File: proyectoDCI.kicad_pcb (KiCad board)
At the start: 2 copper layers, 50 x 30 mm, 27 parts, among them P1 CONN_02X04, P2 CONN_01X01, P3 GSG-RF-CONN, P4 GSG-RF-CONN, U1 AD5933, U2 ADG849, U3 AD8606, U4 ASFLMB-16.000MHZ-LY-T, U5 ADP150

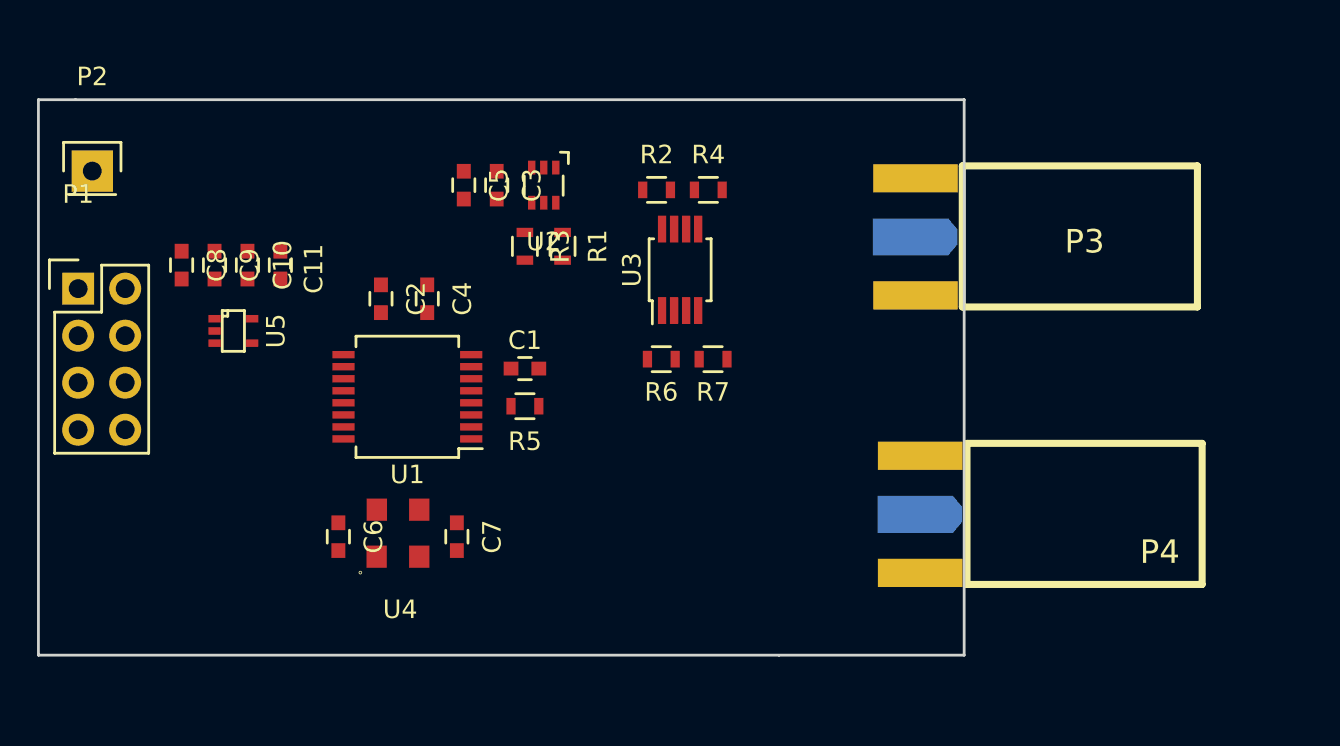
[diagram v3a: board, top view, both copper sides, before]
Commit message: Se achico el tamaño de la placa para hacerla mas compacta
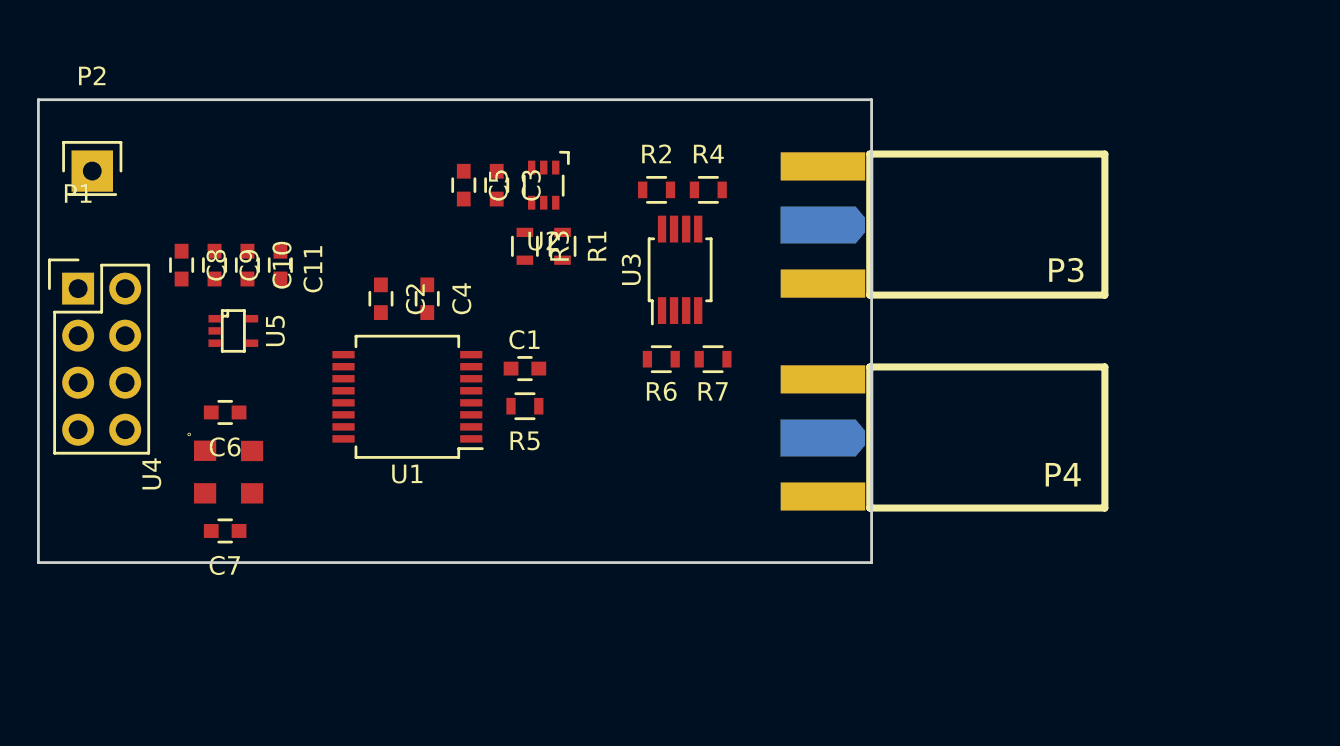
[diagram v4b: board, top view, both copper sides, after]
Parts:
- moved C7 12.5 mm to (160.1, 121.3), turned to 180 degrees
- moved U4 9.72 mm to (160.3, 118.1), turned to 270 degrees
- moved C6 9.08 mm to (160.1, 114.9), turned to 180 degrees
- moved P4 6.68 mm to (201.2, 115.0)
- moved P3 5.04 mm to (201.2, 103.5)
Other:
- board size 50 x 30 mm -> 45 x 25 mm
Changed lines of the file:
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@@
     (area 149.924999 97.924999 200.075001 128.075001)
     (thickness 1.6)
-    (drawings 36)
+    (drawings 34)
     (tracks 0)
     (zones 0)
@@
   )
   (module Capacitors_SMD:C_0603 (layer F.Cu)
-    (at 166.2 121.6 270)
+    (at 160.086 114.892 180)
     (descr "Capacitor SMD 0603, reflow soldering, AVX (see smccp.pdf)")
     (tags "capacitor 0603")
     (attr smd)
-    (fp_text reference C6 (at 0 -1.9 270) (layer F.SilkS)
-      (effects (font (size 1 1) (thickness 0.15)))
-    )
-    (fp_text value 10uF (at 0 1.9 270) (layer F.Fab)
+    (fp_text reference C6 (at 0 -1.9 180) (layer F.SilkS)
+      (effects (font (size 1 1) (thickness 0.15)))
+    )
+    (fp_text value 10uF (at 0 1.9 180) (layer F.Fab)
       (effects (font (size 1 1) (thickness 0.15)))
     )
@@
     (fp_line (start -0.35 -0.6) (end 0.35 -0.6) (layer F.SilkS) (width 0.15))
     (fp_line (start 0.35 0.6) (end -0.35 0.6) (layer F.SilkS) (width 0.15))
-    (pad 1 smd rect (at -0.75 0 270) (size 0.8 0.75) (layers F.Cu F.Paste F.Mask)
+    (pad 1 smd rect (at -0.75 0 180) (size 0.8 0.75) (layers F.Cu F.Paste F.Mask)
       (net 1 VDD))
-    (pad 2 smd rect (at 0.75 0 270) (size 0.8 0.75) (layers F.Cu F.Paste F.Mask)
+    (pad 2 smd rect (at 0.75 0 180) (size 0.8 0.75) (layers F.Cu F.Paste F.Mask)
       (net 2 GND))
     (model Capacitors_SMD.3dshapes/C_0603.wrl
@@
   )
   (module Capacitors_SMD:C_0603 (layer F.Cu)
-    (at 172.6 121.6 270)
+    (at 160.086 121.292 180)
     (descr "Capacitor SMD 0603, reflow soldering, AVX (see smccp.pdf)")
     (tags "capacitor 0603")
     (attr smd)
-    (fp_text reference C7 (at 0 -1.9 270) (layer F.SilkS)
-      (effects (font (size 1 1) (thickness 0.15)))
-    )
-    (fp_text value 0,1uF (at 0 1.9 270) (layer F.Fab)
+    (fp_text reference C7 (at 0 -1.9 180) (layer F.SilkS)
+      (effects (font (size 1 1) (thickness 0.15)))
+    )
+    (fp_text value 0,1uF (at 0 1.9 180) (layer F.Fab)
       (effects (font (size 1 1) (thickness 0.15)))
     )
@@
     (fp_line (start -0.35 -0.6) (end 0.35 -0.6) (layer F.SilkS) (width 0.15))
     (fp_line (start 0.35 0.6) (end -0.35 0.6) (layer F.SilkS) (width 0.15))
-    (pad 1 smd rect (at -0.75 0 270) (size 0.8 0.75) (layers F.Cu F.Paste F.Mask)
+    (pad 1 smd rect (at -0.75 0 180) (size 0.8 0.75) (layers F.Cu F.Paste F.Mask)
       (net 1 VDD))
-    (pad 2 smd rect (at 0.75 0 270) (size 0.8 0.75) (layers F.Cu F.Paste F.Mask)
+    (pad 2 smd rect (at 0.75 0 180) (size 0.8 0.75) (layers F.Cu F.Paste F.Mask)
       (net 2 GND))
     (model Capacitors_SMD.3dshapes/C_0603.wrl
@@
   )
   (module propios:TCXO (layer F.Cu)
-    (at 169.418 121.412)
-    (fp_text reference U4 (at 0.12 4.12) (layer F.SilkS)
-      (effects (font (size 1 1) (thickness 0.15)))
-    )
-    (fp_text value ASFLMB-16.000MHZ-LY-T (at 0.09 2.68) (layer F.Fab)
+    (at 160.274 118.11 270)
+    (fp_text reference U4 (at 0.12 4.12 270) (layer F.SilkS)
+      (effects (font (size 1 1) (thickness 0.15)))
+    )
+    (fp_text value ASFLMB-16.000MHZ-LY-T (at 0.09 2.68 270) (layer F.Fab)
       (effects (font (size 1 1) (thickness 0.15)))
     )
     (fp_circle (center -2.03 2.13) (end -2.01 2.13) (layer F.SilkS) (width 0.15))
-    (pad 1 smd rect (at -1.15 1.27) (size 1.1 1.2) (layers F.Cu F.Paste F.Mask)
-      (net 2 GND))
-    (pad 2 smd rect (at 1.15 1.27) (size 1.1 1.2) (layers F.Cu F.Paste F.Mask)
-      (net 2 GND))
-    (pad 4 smd rect (at -1.14 -1.27) (size 1.1 1.2) (layers F.Cu F.Paste F.Mask)
+    (pad 1 smd rect (at -1.15 1.27 270) (size 1.1 1.2) (layers F.Cu F.Paste F.Mask)
+      (net 2 GND))
+    (pad 2 smd rect (at 1.15 1.27 270) (size 1.1 1.2) (layers F.Cu F.Paste F.Mask)
+      (net 2 GND))
+    (pad 4 smd rect (at -1.14 -1.27 270) (size 1.1 1.2) (layers F.Cu F.Paste F.Mask)
       (net 1 VDD))
-    (pad 3 smd rect (at 1.15 -1.27) (size 1.1 1.2) (layers F.Cu F.Paste F.Mask)
+    (pad 3 smd rect (at 1.15 -1.27 270) (size 1.1 1.2) (layers F.Cu F.Paste F.Mask)
       (net 9 /Otros/MCLK))
   )
@@
   )
   (module SMA_EDGE:SMA_EDGE (layer F.Cu)
-    (at 206.248 104.14)
-    (fp_text reference P3 (at 0.254 1.524) (layer F.SilkS)
+    (at 201.25 103.5)
+    (fp_text reference P3 (at 4.25 3.75) (layer F.SilkS)
       (effects (font (thickness 0.3048)))
     )
@@
   )
   (module SMA_EDGE:SMA_EDGE (layer F.Cu)
-    (at 206.502 119.126)
+    (at 201.25 115)
     (fp_text reference P4 (at 4.064 3.302) (layer F.SilkS)
       (effects (font (thickness 0.3048)))
@@
     )
   )
+  (gr_line (start 150 98) (end 195 98) (angle 90) (layer Edge.Cuts) (width 0.15))
+  (gr_line (start 150 123) (end 195 123) (angle 90) (layer Edge.Cuts) (width 0.15))
+  (gr_line (start 150 123) (end 150 98) (angle 90) (layer Edge.Cuts) (width 0.15))
+  (gr_line (start 195 98) (end 195 123) (angle 90) (layer Edge.Cuts) (width 0.15))
   (gr_text OPAMP (at 184.658 98.806) (layer Cmts.User)
     (effects (font (size 1.5 1.5) (thickness 0.3)))
@@
   (gr_line (start 179.578 107.696) (end 179.578 100.076) (angle 90) (layer Cmts.User) (width 0.2))
   (gr_line (start 174.752 107.696) (end 179.578 107.696) (angle 90) (layer Cmts.User) (width 0.2))
-  (gr_text Reloj (at 172.466 125.984) (layer Cmts.User)
+  (gr_text Reloj (at 160 125) (layer Cmts.User)
     (effects (font (size 1.5 1.5) (thickness 0.3)))
   )
-  (gr_line (start 164.592 118.364) (end 164.592 118.618) (angle 90) (layer Cmts.User) (width 0.2))
-  (gr_line (start 175.26 118.364) (end 164.592 118.364) (angle 90) (layer Cmts.User) (width 0.2))
-  (gr_line (start 175.26 118.618) (end 175.26 118.364) (angle 90) (layer Cmts.User) (width 0.2))
-  (gr_line (start 175.26 124.46) (end 175.26 118.618) (angle 90) (layer Cmts.User) (width 0.2))
-  (gr_line (start 164.592 124.46) (end 175.26 124.46) (angle 90) (layer Cmts.User) (width 0.2))
-  (gr_line (start 164.592 118.364) (end 164.592 124.46) (angle 90) (layer Cmts.User) (width 0.2))
+  (gr_line (start 163.322 113.284) (end 163.068 113.284) (angle 90) (layer Cmts.User) (width 0.2))
+  (gr_line (start 163.322 123.952) (end 163.322 113.284) (angle 90) (layer Cmts.User) (width 0.2))
+  (gr_line (start 163.068 123.952) (end 163.322 123.952) (angle 90) (layer Cmts.User) (width 0.2))
+  (gr_line (start 157.226 123.952) (end 163.068 123.952) (angle 90) (layer Cmts.User) (width 0.2))
+  (gr_line (start 157.226 113.284) (end 157.226 123.952) (angle 90) (layer Cmts.User) (width 0.2))
+  (gr_line (start 163.322 113.284) (end 157.226 113.284) (angle 90) (layer Cmts.User) (width 0.2))
   (gr_text Fuente (at 160.528 103.886) (layer Cmts.User)
     (effects (font (size 1.5 1.5) (thickness 0.3)))
@@
   (gr_line (start 156.718 112.268) (end 164.592 112.268) (angle 90) (layer Cmts.User) (width 0.2))
   (gr_line (start 156.718 105.156) (end 156.718 112.268) (angle 90) (layer Cmts.User) (width 0.2))
-  (gr_line (start 200 105.5) (end 220 105.5) (angle 90) (layer Dwgs.User) (width 0.2))
-  (gr_line (start 200 120.5) (end 220 120.5) (angle 90) (layer Dwgs.User) (width 0.2))
-  (gr_line (start 200 113) (end 220 113) (angle 90) (layer Dwgs.User) (width 0.2))
+  (gr_line (start 195.056 116.23) (end 215.056 116.23) (angle 90) (layer Dwgs.User) (width 0.2))
+  (gr_line (start 195.056 104.73) (end 215.056 104.73) (angle 90) (layer Dwgs.User) (width 0.2))
+  (gr_line (start 195.056 110.73) (end 215.056 110.73) (angle 90) (layer Dwgs.User) (width 0.2))
   (gr_line (start 150 113) (end 141 113) (angle 90) (layer Dwgs.User) (width 0.2))
-  (gr_line (start 150 98) (end 150 128) (angle 90) (layer Edge.Cuts) (width 0.15))
-  (gr_line (start 152 98) (end 150 98) (angle 90) (layer Edge.Cuts) (width 0.15))
-  (gr_line (start 200 98) (end 152 98) (angle 90) (layer Edge.Cuts) (width 0.15))
-  (gr_line (start 200 128) (end 200 98) (angle 90) (layer Edge.Cuts) (width 0.15))
-  (gr_line (start 190 128) (end 200 128) (angle 90) (layer Edge.Cuts) (width 0.15))
-  (gr_line (start 150 128) (end 190 128) (angle 90) (layer Edge.Cuts) (width 0.15))
 )

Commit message: Se achico nuevamente la placa y se acomodo la serigrafia
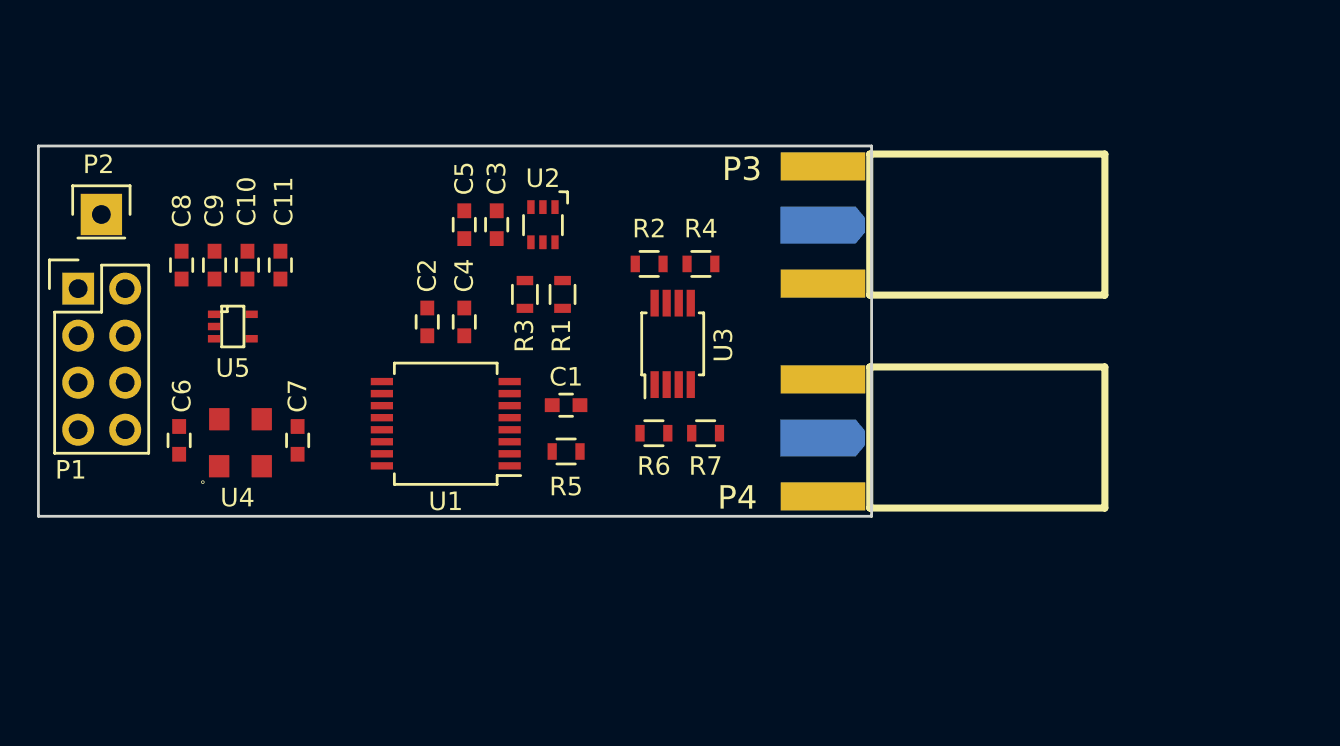
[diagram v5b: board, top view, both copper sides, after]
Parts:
- moved C7 6.27 mm to (164.0, 116.4), turned to 270 degrees
- moved R2 4.02 mm to (183.0, 106.9)
- moved R6 4.02 mm to (183.2, 116.0)
- moved R7 4.02 mm to (186.0, 116.0)
- moved R4 4.02 mm to (185.8, 106.9)
- moved U3 4.02 mm to (184.3, 111.2)
- moved R5 3.31 mm to (178.5, 117.0)
- moved C1 2.98 mm to (178.5, 114.5)
- moved C6 2.91 mm to (157.6, 116.4), turned to 270 degrees
- moved C2 2.80 mm to (171.0, 110.0)
- moved R1 2.60 mm to (178.3, 108.5)
- moved R3 2.60 mm to (176.3, 108.5)
- moved U1 2.53 mm to (172.0, 115.5)
- moved P2 2.40 mm to (153.4, 104.2)
- moved C4 2.36 mm to (173.0, 110.0)
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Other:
- board size 45 x 25 mm -> 45 x 20 mm
- board text added: "Medidor"

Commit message: Antes de comenzar a rutear. Reglas cargadas
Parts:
- moved C7 10.5 mm to (159.6, 106.9)
- moved C10 10.1 mm to (164.2, 116.6)
- moved C6 9.50 mm to (157.6, 106.9)
- moved C8 9.47 mm to (157.8, 116.4)
- moved C9 2.09 mm to (161.6, 106.9)
- moved C11 0.53 mm to (163.6, 106.9)
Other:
- net class Default: clearance 0.2 -> 0.15; trace_width 0.25 -> 0.15; via_dia 0.6 -> 0.7
- rule trace_clearance: 0.2 -> 0.15
- rule trace_min: 0.2 -> 0.15
- rule via_min_drill: 0.3 -> 0.4
- rule via_min_size: 0.4 -> 0.7
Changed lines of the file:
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@@
   )
   (setup
-    (last_trace_width 0.25)
-    (trace_clearance 0.2)
+    (last_trace_width 0.15)
+    (user_trace_width 0.15)
+    (user_trace_width 0.3)
+    (trace_clearance 0.15)
     (zone_clearance 0.508)
     (zone_45_only no)
-    (trace_min 0.2)
+    (trace_min 0.15)
     (segment_width 0.2)
     (edge_width 0.15)
-    (via_size 0.6)
+    (via_size 0.7)
     (via_drill 0.4)
-    (via_min_size 0.4)
-    (via_min_drill 0.3)
+    (via_min_size 0.7)
+    (via_min_drill 0.4)
+    (user_via 0.7 0.4)
     (uvia_size 0.3)
     (uvia_drill 0.1)
@@
   (net 17 /Senal/VCC)
   (net_class Default "This is the default net class."
-    (clearance 0.2)
-    (trace_width 0.25)
-    (via_dia 0.6)
+    (clearance 0.15)
+    (trace_width 0.15)
+    (via_dia 0.7)
     (via_drill 0.4)
     (uvia_dia 0.3)
@@
   )
   (module Capacitors_SMD:C_0603 (layer F.Cu)
-    (at 157.6 116.4 270)
+    (at 157.6 106.9 270)
     (descr "Capacitor SMD 0603, reflow soldering, AVX (see smccp.pdf)")
     (tags "capacitor 0603")
@@
   )
   (module Capacitors_SMD:C_0603 (layer F.Cu)
-    (at 164 116.4 270)
+    (at 159.6 106.9 270)
     (descr "Capacitor SMD 0603, reflow soldering, AVX (see smccp.pdf)")
     (tags "capacitor 0603")
@@
   )
   (module Capacitors_SMD:C_0603 (layer F.Cu)
-    (at 157.734 106.934 270)
-    (descr "Capacitor SMD 0603, reflow soldering, AVX (see smccp.pdf)")
-    (tags "capacitor 0603")
-    (attr smd)
-    (fp_text reference C8 (at -2.934 -0.016 270) (layer F.SilkS)
+    (at 157.8 116.4 270)
+    (descr "Capacitor SMD 0603, reflow soldering, AVX (see smccp.pdf)")
+    (tags "capacitor 0603")
+    (attr smd)
+    (fp_text reference C8 (at -2.5 0 270) (layer F.SilkS)
       (effects (font (size 1 1) (thickness 0.15)))
     )
@@
   )
   (module Capacitors_SMD:C_0603 (layer F.Cu)
-    (at 159.512 106.934 270)
-    (descr "Capacitor SMD 0603, reflow soldering, AVX (see smccp.pdf)")
-    (tags "capacitor 0603")
-    (attr smd)
-    (fp_text reference C9 (at -2.934 0.012 270) (layer F.SilkS)
+    (at 161.6 106.9 270)
+    (descr "Capacitor SMD 0603, reflow soldering, AVX (see smccp.pdf)")
+    (tags "capacitor 0603")
+    (attr smd)
+    (fp_text reference C9 (at -2.4 0 270) (layer F.SilkS)
       (effects (font (size 1 1) (thickness 0.15)))
     )
@@
   )
   (module Capacitors_SMD:C_0603 (layer F.Cu)
-    (at 161.29 106.934 270)
-    (descr "Capacitor SMD 0603, reflow soldering, AVX (see smccp.pdf)")
-    (tags "capacitor 0603")
-    (attr smd)
-    (fp_text reference C10 (at -3.434 0.04 270) (layer F.SilkS)
+    (at 164.2 116.6 270)
+    (descr "Capacitor SMD 0603, reflow soldering, AVX (see smccp.pdf)")
+    (tags "capacitor 0603")
+    (attr smd)
+    (fp_text reference C10 (at -3 0 270) (layer F.SilkS)
       (effects (font (size 1 1) (thickness 0.15)))
     )
@@
   )
   (module Capacitors_SMD:C_0603 (layer F.Cu)
-    (at 163.068 106.934 270)
-    (descr "Capacitor SMD 0603, reflow soldering, AVX (see smccp.pdf)")
-    (tags "capacitor 0603")
-    (attr smd)
-    (fp_text reference C11 (at -3.434 -0.182 270) (layer F.SilkS)
+    (at 163.6 106.9 270)
+    (descr "Capacitor SMD 0603, reflow soldering, AVX (see smccp.pdf)")
+    (tags "capacitor 0603")
+    (attr smd)
+    (fp_text reference C11 (at -2.9 -0.1 270) (layer F.SilkS)
       (effects (font (size 1 1) (thickness 0.15)))
     )
@@
     (descr "Through hole pin header")
     (tags "pin header")
-    (fp_text reference P2 (at -0.15 -2.7) (layer F.SilkS)
-      (effects (font (size 1 1) (thickness 0.15)))
-    )
+    (fp_text reference P2 (at 0 -2.4) (layer F.SilkS)
+      (effects (font (size 1 1) (thickness 0.15)))
+    )
